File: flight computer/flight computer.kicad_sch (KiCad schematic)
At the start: 49 parts, among them IC1 114993390, J1 SMA-J-P-H-ST-EM1, J2 SMA-J-P-H-ST-EM1, Q1 BSS138, Q2 BSS84, U1 TPS56A37RPAR, U2 BMP581, U3 BNO086, U4 BTM9011EP, U5 RP2354B, U6 MAX-M10S-00B, U8 VND9025AJTR, U9 74LVC1G07GW_125

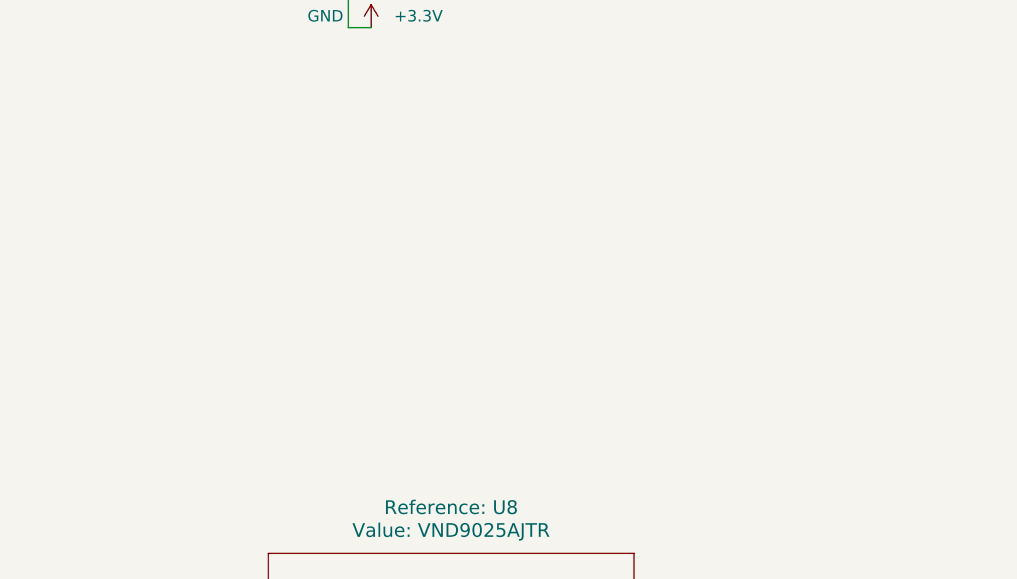
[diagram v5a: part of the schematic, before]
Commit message: AZ1117CH 3.3V LDO added
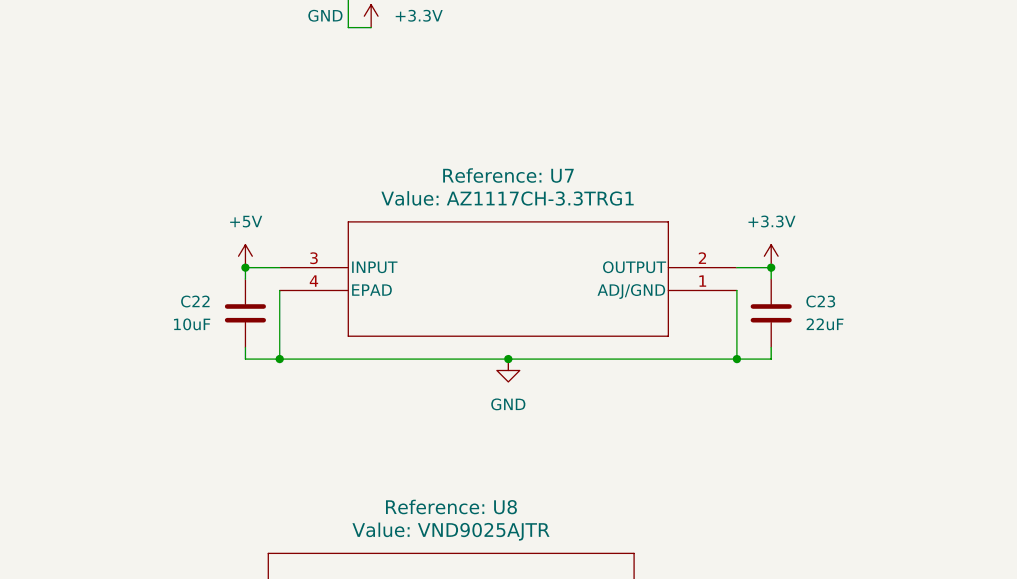
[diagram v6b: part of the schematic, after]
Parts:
- added C22: 10uF, Capacitor_SMD:C_1206_3216Metric_Pad1.33x1.80mm_HandSolder, symbol Device:C
- added C23: 22uF, Capacitor_SMD:C_1210_3225Metric_Pad1.33x2.70mm_HandSolder, symbol Device:C
- added U7: AZ1117CH-3.3TRG1, Snapeda:SOT-223_DIO-L, symbol Snapeda:AZ1117CH-3.3TRG1
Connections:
- net +3.3V: now also C23.2, U7.2 (OUTPUT)
- net +5V: now also C22.2, U7.3 (INPUT)
- net GND: now also C22.1, C23.1, U7.1 (ADJ/GND), U7.4 (EPAD)

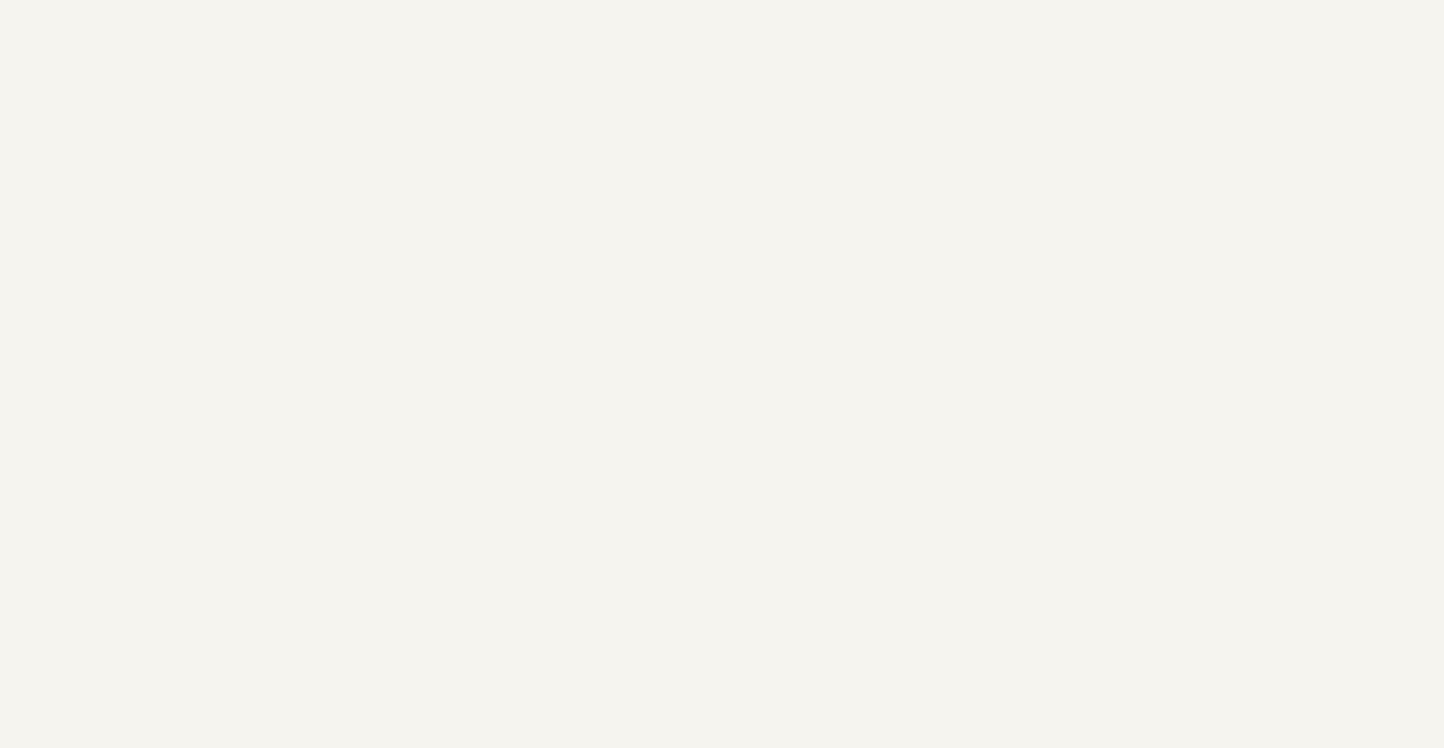
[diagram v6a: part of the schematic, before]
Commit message: On/Off circuit added
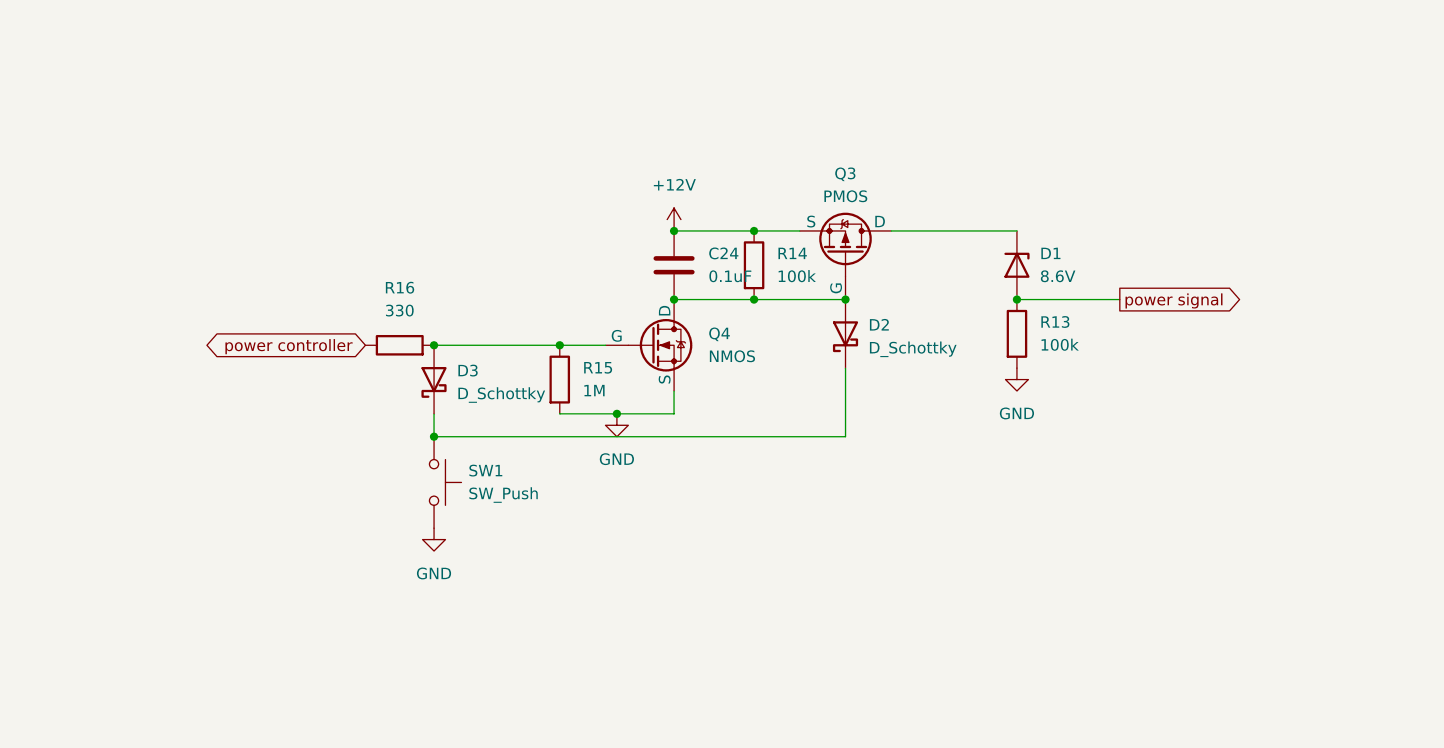
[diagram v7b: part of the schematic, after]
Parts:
- added C24: 0.1uF, symbol Device:C
- added D1: 8.6V, symbol Device:D_Zener
- added D2, D3: D_Schottky, symbol Device:D_Schottky
- added Q3: PMOS, symbol Simulation_SPICE:PMOS
- added Q4: NMOS, symbol Simulation_SPICE:NMOS
- added R13, R14: 100k, symbol Device:R
- added R15: 1M, symbol Device:R
- added R16: 330, symbol Device:R
- added SW1: SW_Push, symbol Switch:SW_Push
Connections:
- net +12V: now also C24.1, Q3.3 (S), R14.1
- net GND: now also Q4.3 (S), R13.2, R15.2, SW1.1
- new net: C24.2, D2.2 (A), Q3.2 (G), Q4.1 (D), R14.2
- new net: D3.2 (A), Q4.2 (G), R15.1, R16.2
- new net: D2.1 (K), D3.1 (K), SW1.2
- new net: D1.1 (K), Q3.1 (D)
- new net power controller: R16.1
- new net power signal: D1.2 (A), R13.1

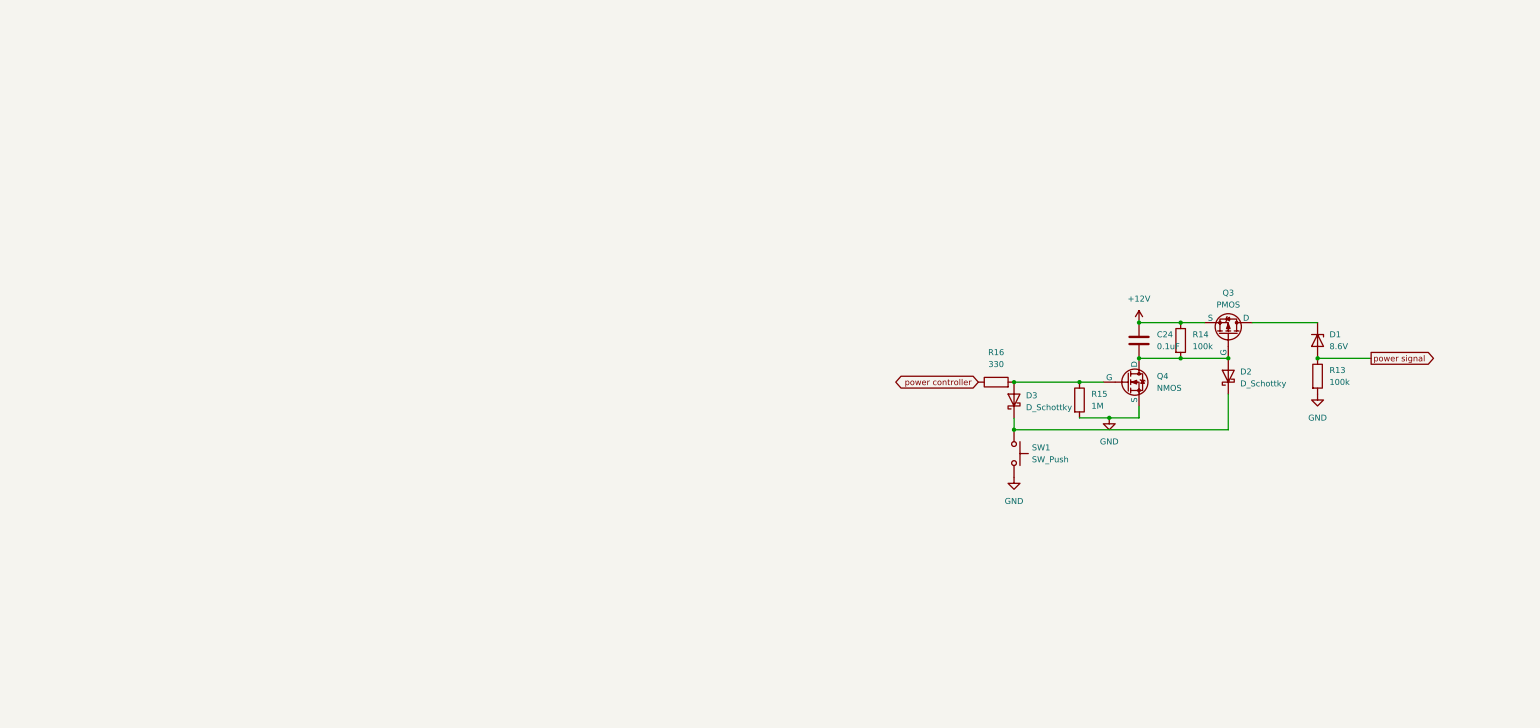
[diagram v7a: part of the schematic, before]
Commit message: ADXL375 accelerometer added
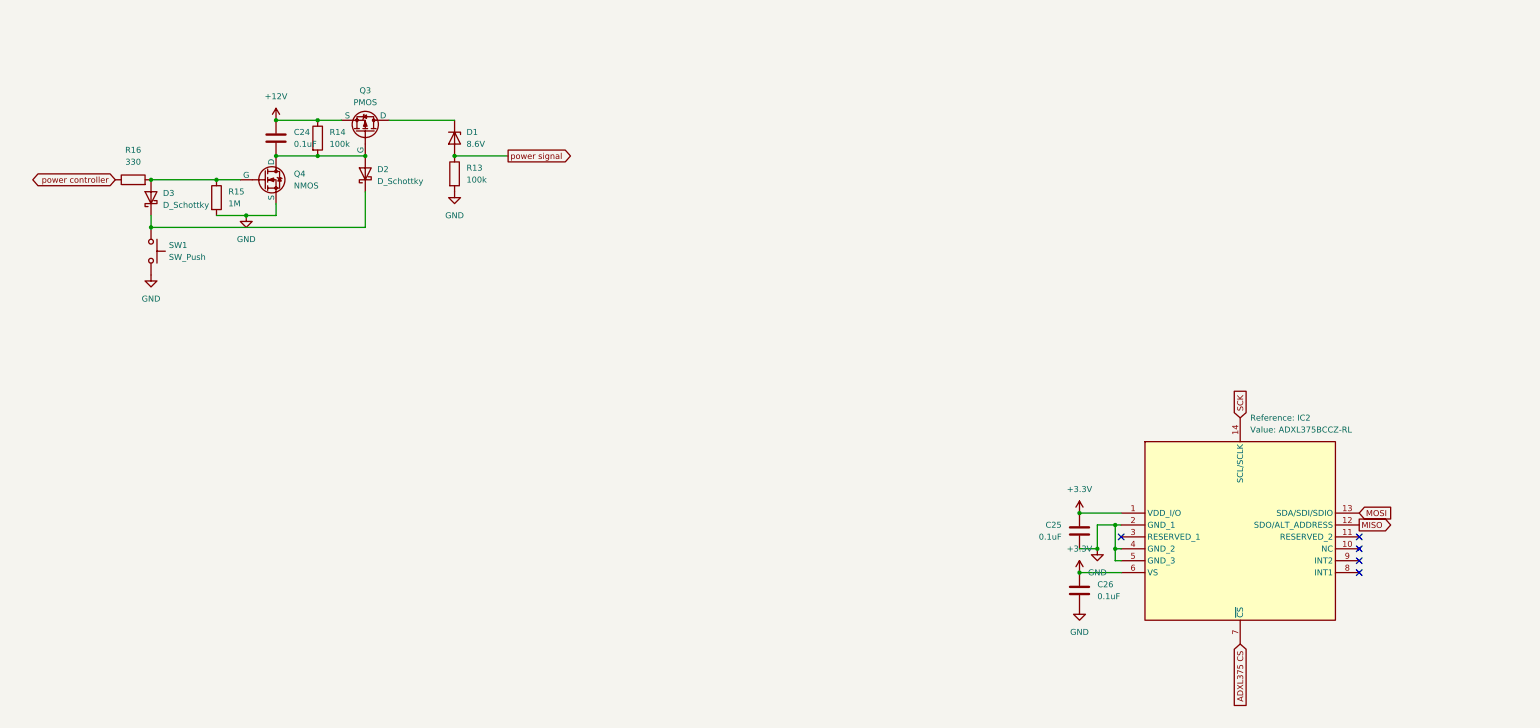
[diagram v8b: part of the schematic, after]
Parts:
- added C25, C26: 0.1uF, Capacitor_SMD:C_0805_2012Metric_Pad1.18x1.45mm_HandSolder, symbol Device:C
- added IC2: ADXL375BCCZ-RL, Samacsys:ADXL375BCCZRL, symbol Samacsys:ADXL375BCCZ-RL
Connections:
- net +3.3V: now also C25.1, C26.1, IC2.1 (VDD_I/O), IC2.6 (VS)
- net GND: now also C25.2, C26.2, IC2.2 (GND_1), IC2.4 (GND_2), IC2.5 (GND_3)
- net MISO: now also IC2.12 (SDO/ALT_ADDRESS)
- net MOSI: now also IC2.13 (SDA/SDI/SDIO)
- net SCK: now also IC2.14 (SCL/SCLK)
- new net ADXL375 CS: IC2.7 (~{CS})
- no-connect marks 11 -> 16
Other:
- moved on the sheet: C24, D1, D2, D3, Q3, Q4, R13, R14, R15, R16, SW1
